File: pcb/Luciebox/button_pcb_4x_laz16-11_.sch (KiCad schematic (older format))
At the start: 48 parts, among them T1 terminal_8x1, T2 terminal_8x1, T3 terminal_8x1, T4 terminal_8x1, T5 terminal_8x1, T6 terminal_8x1, U1 4digit_7segments_common_anode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

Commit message: button board pcb v1.0 + gerbers
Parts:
- added H13, H14, H15, H? (x2): MountingHole, Luciebox:MountingHole_4.3mm_M4, symbol Luciebox_components:MountingHole
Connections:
- net GND: now also R1.6, R1.7, R1.8, R1.9 (LSB), R10.2, R19.6, R19.7, R19.8, R19.9 (LSB), R4.2, R6.2, R8.2, T2.1, T2.2, T2.3, T2.4, T4.1, T4.2, T4.3, T4.4
- net at S1.4 (LED_+), S2.4 (LED_+), S3.4 (LED_+)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: now also S5.4 (LED_+), S6.4 (LED_+), S7.4 (LED_+), S8.4 (LED_+), T3.4, connect_for_vcc_as_common_anode2.2
- net E: now reaches U1.1 (e)
- net E: now also T6.2
- net F: now reaches U1.10 (f)
- net F: now also T5.4
- net A: now reaches U1.11 (a)
- net A: now also T5.3
- net Digit1: now reaches U1.12 (CA1)
- net Digit1: now also T5.2
- net D: now reaches U1.2 (d)
- net D: now also T6.3
- net DP: now reaches U1.3 (DPX)
- net DP: now also T6.4
- net C: now reaches U1.4 (c)
- net C: now also T6.5
- net G: now reaches U1.5 (g)
- net G: now also T6.6
- net Digit4: now reaches U1.6 (CA4)
- net Digit4: now also T6.7
- net B: now reaches U1.7 (b)
- net B: now also T5.7
- net Digit3: now reaches U1.8 (CA3)
- net Digit3: now also T5.6
- net Digit2: now reaches U1.9 (CA2)
- net Digit2: now also T5.5
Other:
- moved on the sheet: T5, T6

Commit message: before finishing v3
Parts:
- gave numbers to parts that had none: 2
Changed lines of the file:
@@
 $EndComp
 $Comp
-L Luciebox_components:MountingHole H?
+L Luciebox_components:MountingHole H16
 U 1 1 5FFEBD74
 P 1800 7650
-F 0 "H?" H 1900 7696 50  0000 L CNN
+F 0 "H16" H 1900 7696 50  0000 L CNN
 F 1 "MountingHole" H 1900 7605 50  0000 L CNN
 F 2 "Luciebox:MountingHole_4.3mm_M4" H 1800 7650 50  0001 C CNN
@@
 $EndComp
 $Comp
-L Luciebox_components:MountingHole H?
+L Luciebox_components:MountingHole H17
 U 1 1 5FFEC049
 P 2050 7650
-F 0 "H?" H 2150 7696 50  0000 L CNN
+F 0 "H17" H 2150 7696 50  0000 L CNN
 F 1 "MountingHole" H 2150 7605 50  0000 L CNN
 F 2 "Luciebox:MountingHole_4.3mm_M4" H 2050 7650 50  0001 C CNN

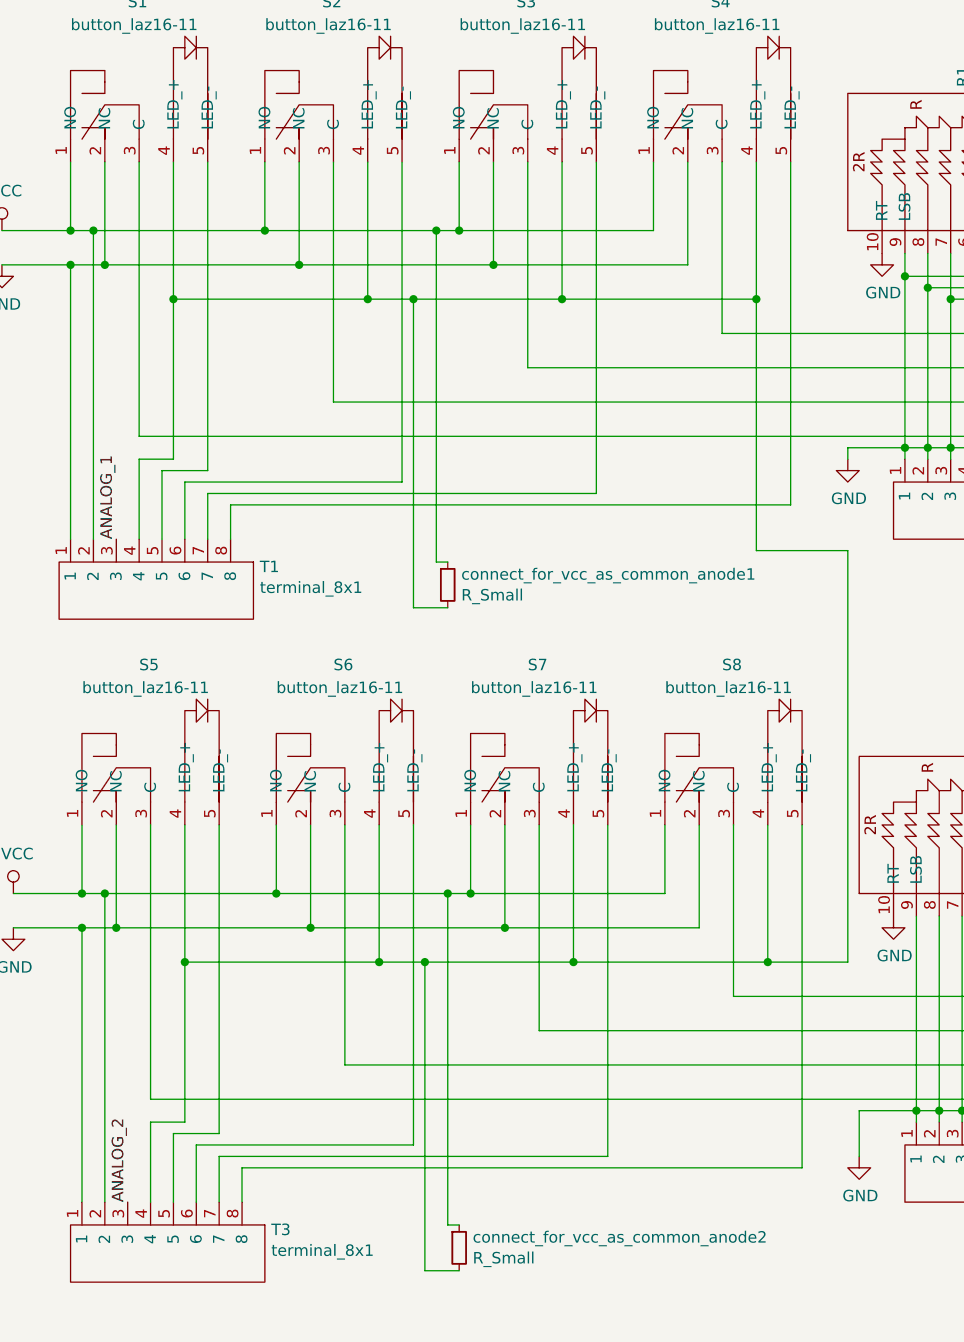
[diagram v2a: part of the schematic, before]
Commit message: correct and send out button board v1.1
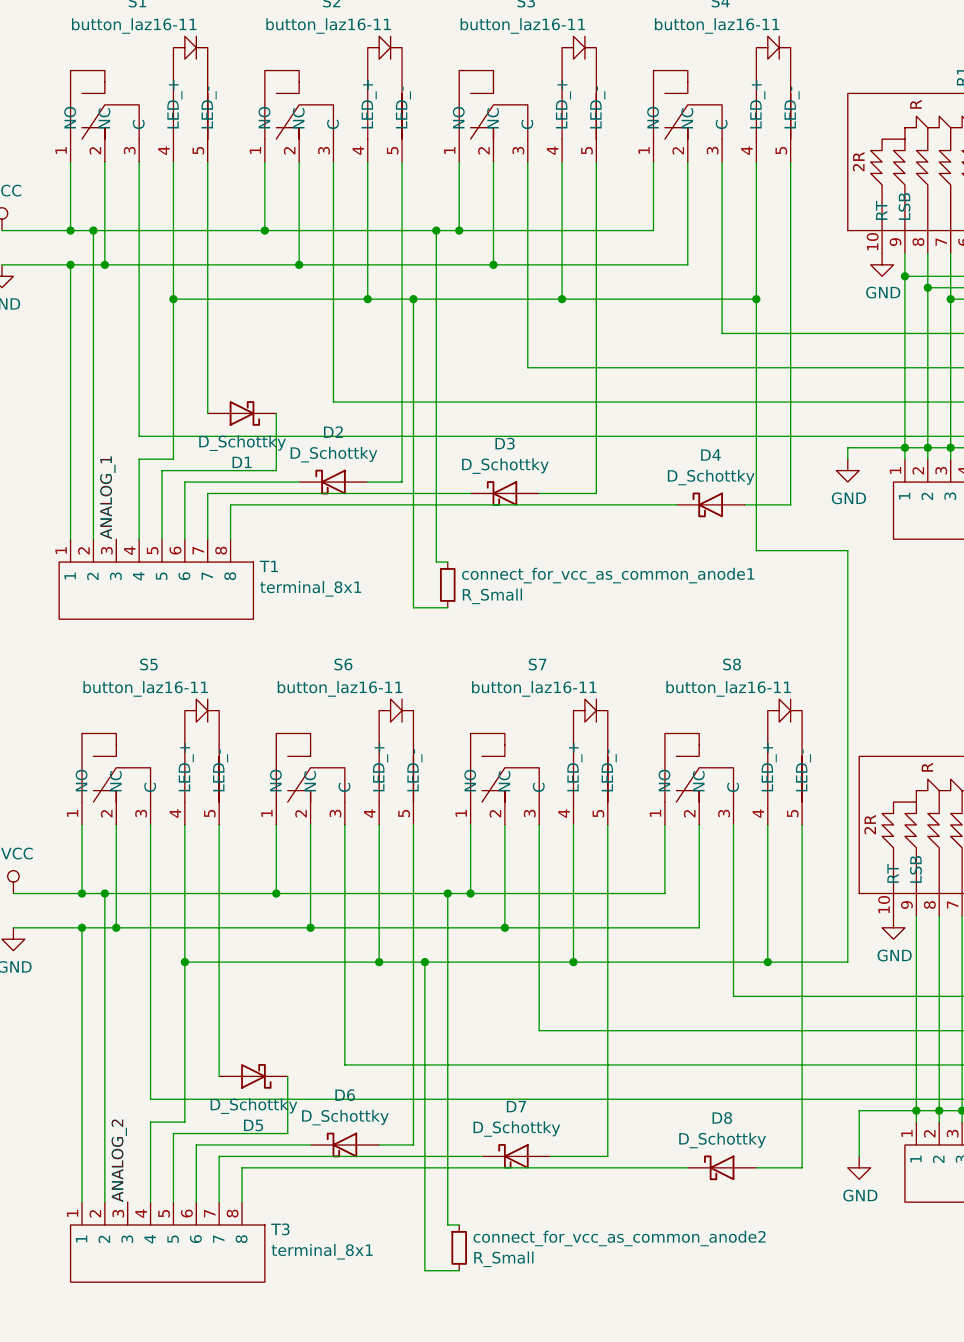
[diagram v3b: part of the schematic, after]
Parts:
- added D1, D2, D3, D4, D5, D6, D7, D8: D_Schottky, Luciebox:smd_throughhole_2_pins, symbol Luciebox_components:D_Schottky
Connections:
- net at S1.5 (LED_-): now also D1.2 (A); no longer T1.5
- net at S2.5 (LED_-): now also D2.2 (A); no longer T1.6
- net at S3.5 (LED_-): now also D3.2 (A); no longer T1.7
- net at S4.5 (LED_-): now also D4.2 (A); no longer T1.8
- net at T3.5: now also D5.1 (K); no longer S5.5 (LED_-)
- net at T3.6: now also D6.1 (K); no longer S6.5 (LED_-)
- net at T3.7: now also D7.1 (K); no longer S7.5 (LED_-)
- net at T3.8: now also D8.1 (K); no longer S8.5 (LED_-)
- new net: D1.1 (K), T1.5
- new net: D2.1 (K), T1.6
- new net: D3.1 (K), T1.7
- new net: D4.1 (K), T1.8
- new net: D8.2 (A), S8.5 (LED_-)
- new net: D7.2 (A), S7.5 (LED_-)
- new net: D6.2 (A), S6.5 (LED_-)
- new net: D5.2 (A), S5.5 (LED_-)
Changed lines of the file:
@@
 	1400 2950 1400 2650
 Wire Wire Line
-	1400 2650 1600 2650
-Wire Wire Line
-	1600 2650 1600 1300
-Wire Wire Line
 	2450 1300 2450 2700
 Wire Wire Line
-	2450 2700 1500 2700
-Wire Wire Line
 	1500 2700 1500 2950
 Wire Wire Line
 	1600 2950 1600 2750
 Wire Wire Line
-	1600 2750 3300 2750
-Wire Wire Line
 	3300 2750 3300 1300
-Wire Wire Line
-	1700 2950 1700 2800
-Wire Wire Line
-	1700 2800 4150 2800
 Wire Wire Line
 	4150 2800 4150 1300
@@
 	5400 4600 5400 5400
 Wire Wire Line
-	5400 5400 1350 5400
-Wire Wire Line
 	1350 4200 1350 5400
 $Comp
@@
 	1450 5850 1450 5550
 Wire Wire Line
-	1450 5550 1650 5550
-Wire Wire Line
-	1650 5550 1650 4200
-Wire Wire Line
 	2500 4200 2500 5600
 Wire Wire Line
-	2500 5600 1550 5600
-Wire Wire Line
 	1550 5600 1550 5850
 Wire Wire Line
 	1650 5850 1650 5650
 Wire Wire Line
-	1650 5650 3350 5650
-Wire Wire Line
 	3350 5650 3350 4200
 Wire Wire Line
 	1750 5850 1750 5700
-Wire Wire Line
-	1750 5700 4200 5700
 Wire Wire Line
 	4200 5700 4200 4200
@@
 	1    0    0    -1
 $EndComp
+Wire Wire Line
+	5400 5400 1350 5400
+Wire Wire Line
+	1650 5300 1650 4200
+Wire Wire Line
+	1950 5300 1950 5550
+Wire Wire Line
+	1950 5550 1450 5550
+Wire Wire Line
+	4000 5700 4200 5700
+Wire Wire Line
+	3700 5700 1750 5700
+Wire Wire Line
+	1650 5650 2800 5650
+Wire Wire Line
+	3100 5650 3350 5650
+Wire Wire Line
+	2500 5600 2350 5600
+Wire Wire Line
+	2050 5600 1550 5600
+Wire Wire Line
+	3950 2800 4150 2800
+Wire Wire Line
+	3650 2800 1700 2800
+Wire Wire Line
+	1600 2750 2750 2750
+Wire Wire Line
+	3050 2750 3300 2750
+Wire Wire Line
+	2450 2700 2300 2700
+Wire Wire Line
+	2000 2700 1500 2700
+Wire Wire Line
+	1700 2950 1700 2800
+Wire Wire Line
+	1600 2400 1600 1300
+Wire Wire Line
+	1900 2400 1900 2650
+Wire Wire Line
+	1900 2650 1400 2650
+$Comp
+L Luciebox_components:D_Schottky D2
+U 1 1 5FD8A338
+P 2150 2700
+F 0 "D2" H 2150 2916 50  0000 C CNN
+F 1 "D_Schottky" H 2150 2825 50  0000 C CNN
+F 2 "Luciebox:smd_throughhole_2_pins" H 2150 2700 50  0001 C CNN
+F 3 "~" H 2150 2700 50  0001 C CNN
+	1    2150 2700
+	1    0    0    -1
+$EndComp
+$Comp
+L Luciebox_components:D_Schottky D3
+U 1 1 5FD8B35D
+P 2900 2750
+F 0 "D3" H 2900 2966 50  0000 C CNN
+F 1 "D_Schottky" H 2900 2875 50  0000 C CNN
+F 2 "Luciebox:smd_throughhole_2_pins" H 2900 2750 50  0001 C CNN
+F 3 "~" H 2900 2750 50  0001 C CNN
+	1    2900 2750
+	1    0    0    -1
+$EndComp
+$Comp
+L Luciebox_components:D_Schottky D4
+U 1 1 5FD8B78C
+P 3800 2800
+F 0 "D4" H 3800 3016 50  0000 C CNN
+F 1 "D_Schottky" H 3800 2925 50  0000 C CNN
+F 2 "Luciebox:smd_throughhole_2_pins" H 3800 2800 50  0001 C CNN
+F 3 "~" H 3800 2800 50  0001 C CNN
+	1    3800 2800
+	1    0    0    -1
+$EndComp
+$Comp
+L Luciebox_components:D_Schottky D1
+U 1 1 5FD8BA17
+P 1750 2400
+F 0 "D1" H 1750 2616 50  0000 C CNN
+F 1 "D_Schottky" H 1750 2525 50  0000 C CNN
+F 2 "Luciebox:smd_throughhole_2_pins" H 1750 2400 50  0001 C CNN
+F 3 "~" H 1750 2400 50  0001 C CNN
+	1    1750 2400
+	-1   0    0    1
+$EndComp
+$Comp
+L Luciebox_components:D_Schottky D8
+U 1 1 5FD8C5EE
+P 3850 5700
+F 0 "D8" H 3850 5916 50  0000 C CNN
+F 1 "D_Schottky" H 3850 5825 50  0000 C CNN
+F 2 "Luciebox:smd_throughhole_2_pins" H 3850 5700 50  0001 C CNN
+F 3 "~" H 3850 5700 50  0001 C CNN
+	1    3850 5700
+	1    0    0    -1
+$EndComp
+$Comp
+L Luciebox_components:D_Schottky D7
+U 1 1 5FD8CD51
+P 2950 5650
+F 0 "D7" H 2950 5866 50  0000 C CNN
+F 1 "D_Schottky" H 2950 5775 50  0000 C CNN
+F 2 "Luciebox:smd_throughhole_2_pins" H 2950 5650 50  0001 C CNN
+F 3 "~" H 2950 5650 50  0001 C CNN
+	1    2950 5650
+	1    0    0    -1
+$EndComp
+$Comp
+L Luciebox_components:D_Schottky D6
+U 1 1 5FD8D11C
+P 2200 5600
+F 0 "D6" H 2200 5816 50  0000 C CNN
+F 1 "D_Schottky" H 2200 5725 50  0000 C CNN
+F 2 "Luciebox:smd_throughhole_2_pins" H 2200 5600 50  0001 C CNN
+F 3 "~" H 2200 5600 50  0001 C CNN
+	1    2200 5600
+	1    0    0    -1
+$EndComp
+$Comp
+L Luciebox_components:D_Schottky D5
+U 1 1 5FD8D54B
+P 1800 5300
+F 0 "D5" H 1800 5516 50  0000 C CNN
+F 1 "D_Schottky" H 1800 5425 50  0000 C CNN
+F 2 "Luciebox:smd_throughhole_2_pins" H 1800 5300 50  0001 C CNN
+F 3 "~" H 1800 5300 50  0001 C CNN
+	1    1800 5300
+	-1   0    0    1
+$EndComp
 $EndSCHEMATC
